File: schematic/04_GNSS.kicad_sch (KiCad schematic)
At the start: 12 parts, among them J5 U.FL_GNSS, J6 SWF_GNSS

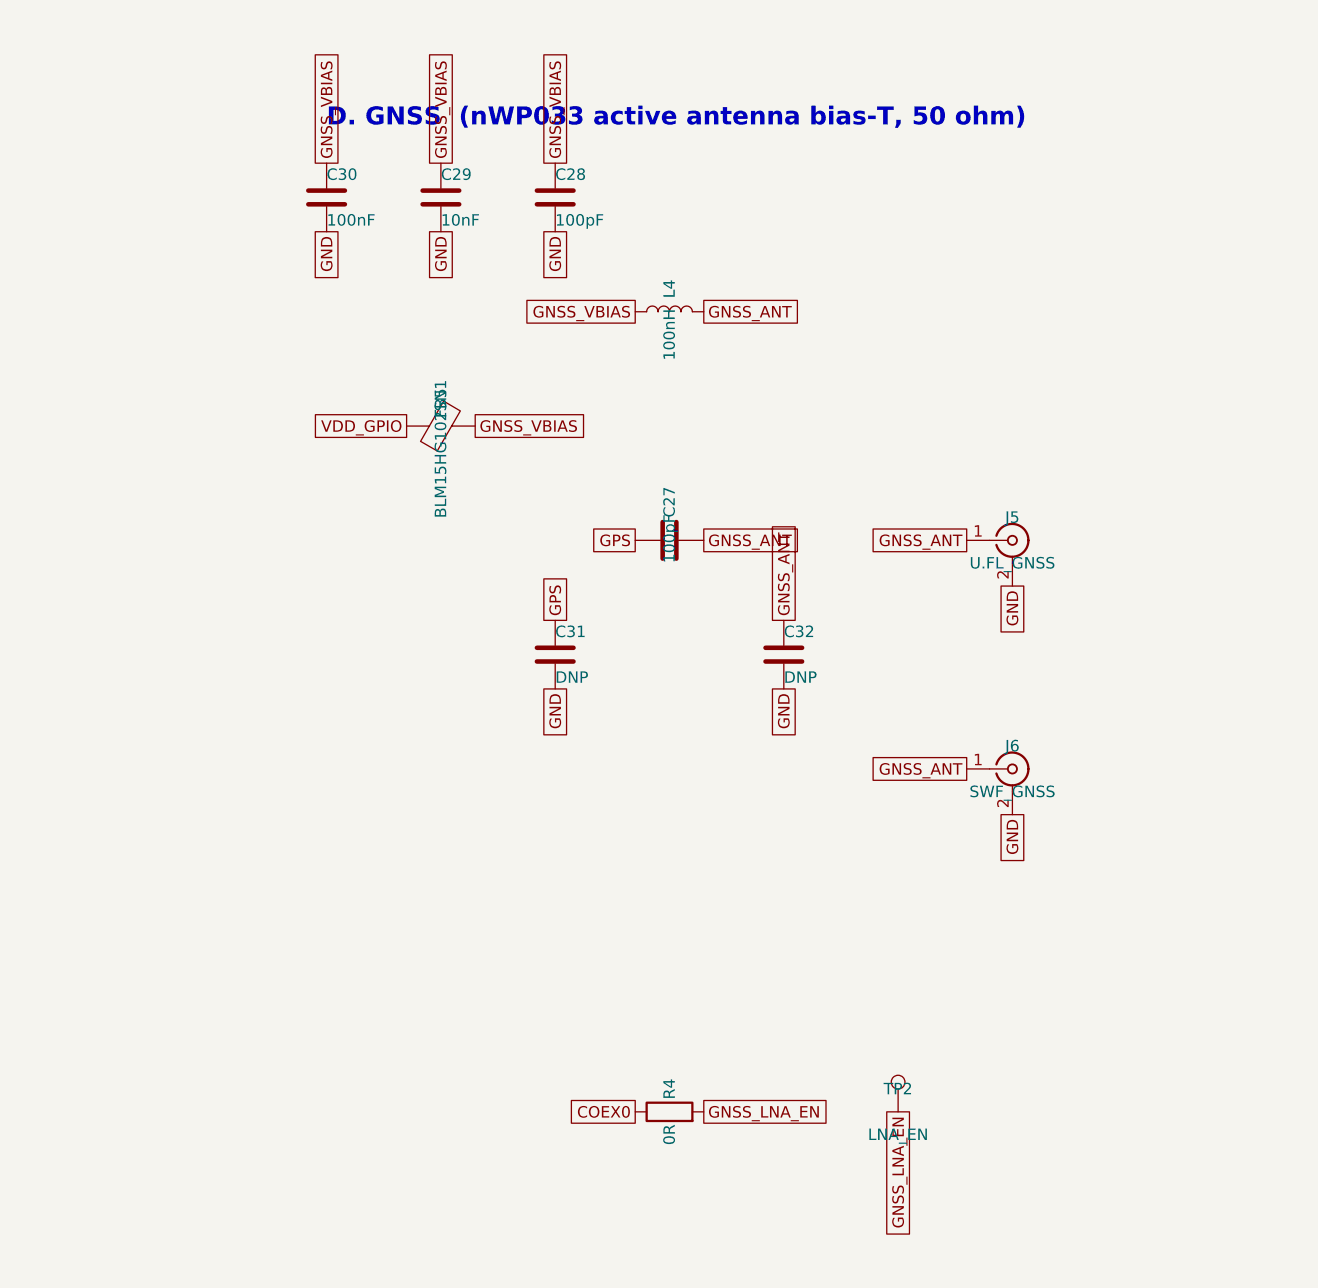
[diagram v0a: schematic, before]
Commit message: Schematic: GNSS COEX0 bias switch, 3.3V VDD_GPIO, DNP RF shunts
- Add U3 TPS22919DCKR on 04_GNSS (COEX0-gated bias); FB5 0402
- Swap U2 to TLV73333 (3.3 V VDD_GPIO); DNP Class-C shunt caps
- Quarantine leftover schematics/; remove stale ERC rpt
- Add PM/DFM/RF/schematic/layout review docs under docs/
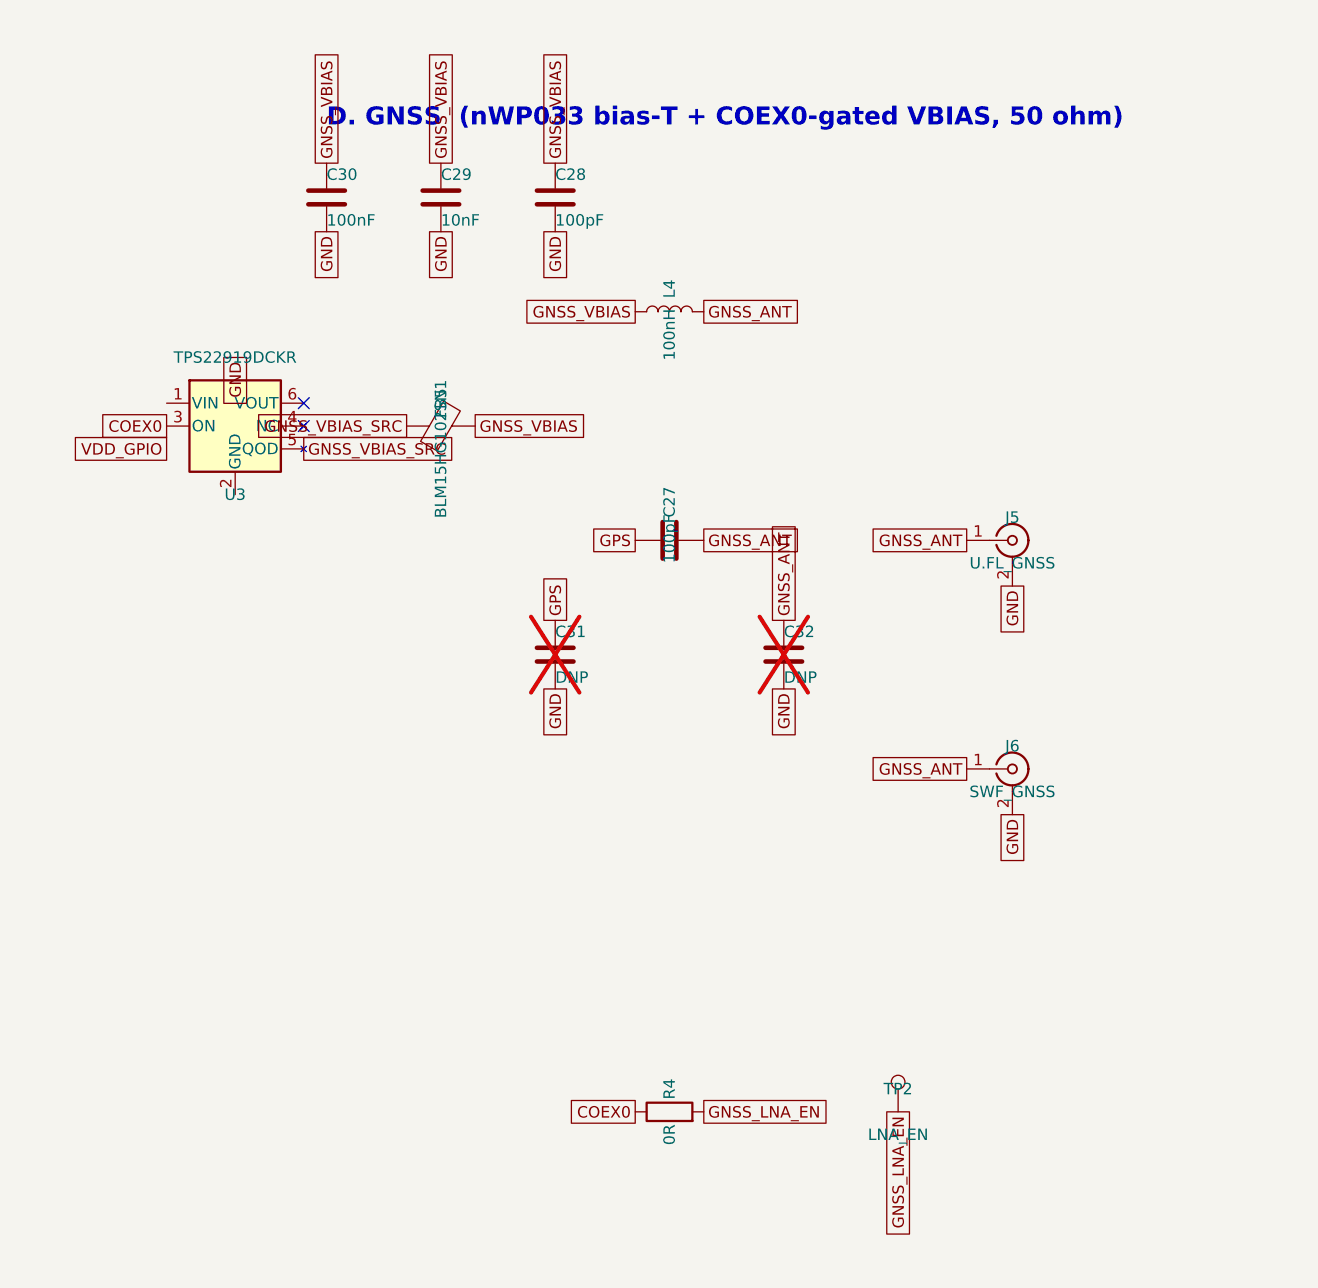
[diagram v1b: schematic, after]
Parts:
- added U3: TPS22919DCKR, Package_TO_SOT_SMD:SOT-363_SC-70-6, symbol power_switch:TPS22919DCK
- C31, C32: now not fitted; now left out of the parts list
- FB5: footprint Inductor_SMD:L_0603_1608Metric -> Inductor_SMD:L_0402_1005Metric
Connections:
- net COEX0: now also U3.3 (ON)
- net VDD_GPIO: no longer FB5.1
- new net GNSS_VBIAS_SRC: FB5.1, U3.5 (QOD)
- no-connect marks 0 -> 2
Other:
- note added: "D. GNSS (nWP033 bias-T + COEX0-gated VBIAS, 50 ohm)"
- note removed: "D. GNSS (nWP033 active antenna bias-T, 50 ohm)"
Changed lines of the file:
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@@
 			)
 		)
-		(property "Footprint" "Inductor_SMD:L_0603_1608Metric"
+		(property "Footprint" "Inductor_SMD:L_0402_1005Metric"
 			(at 38.1 39.878 90)
 			(hide yes)
@@
 		(unit 1)
 		(exclude_from_sim no)
-		(in_bom yes)
+		(in_bom no)
 		(on_board yes)
-		(dnp no)
+		(dnp yes)
 		(property "Reference" "C31"
 			(at 50.8 60.96 0)
@@
 		(unit 1)
 		(exclude_from_sim no)
-		(in_bom yes)
+		(in_bom no)
 		(on_board yes)
-		(dnp no)
+		(dnp yes)
 		(property "Reference" "C32"
 			(at 76.2 60.96 0)
@@
 		)
 	)
-	(global_label "VDD_GPIO"
+	(global_label "GNSS_VBIAS_SRC"
 		(at 34.29 38.1 180)
 		(effects
@@
 		)
 	)
-	(text "D. GNSS  (nWP033 active antenna bias-T, 50 ohm)"
+	(symbol
+		(lib_id "power_switch:TPS22919DCK")
+		(at 15.24 38.1 0)
+		(unit 1)
+		(exclude_from_sim no)
+		(in_bom yes)
+		(on_board yes)
+		(dnp no)
+		(property "Reference" "U3"
+			(at 15.24 45.72 0)
+			(show_name no)
+			(do_not_autoplace no)
+			(effects
+				(font
+					(size 1.27 1.27)
+				)
+			)
+		)
+		(property "Value" "TPS22919DCKR"
+			(at 15.24 30.48 0)
+			(show_name no)
+			(do_not_autoplace no)
+			(effects
+				(font
+					(size 1.27 1.27)
+				)
+			)
+		)
+		(property "Footprint" "Package_TO_SOT_SMD:SOT-363_SC-70-6"
+			(at 15.24 38.1 0)
+			(hide yes)
+			(show_name no)
+			(do_not_autoplace no)
+			(effects
+				(font
+					(size 1.27 1.27)
+				)
+			)
+		)
+		(property "Datasheet" "https://www.ti.com/lit/ds/symlink/tps22919.pdf"
+			(at 15.24 38.1 0)
+			(hide yes)
+			(show_name no)
+			(do_not_autoplace no)
+			(effects
+				(font
+					(size 1.27 1.27)
+				)
+			)
+		)
+		(property "Description" "GNSS VBIAS high-side load switch; EN=COEX0"
+			(at 15.24 38.1 0)
+			(hide yes)
+			(show_name no)
+			(do_not_autoplace no)
+			(effects
+				(font
+					(size 1.27 1.27)
+				)
+			)
+		)
+		(pin "1"
+		)
+		(pin "2"
+		)
+		(pin "3"
+		)
+		(pin "4"
+		)
+		(pin "5"
+		)
+		(pin "6"
+		)
+		(instances
+			(project "nRF9161-DEV-BOARD"
+				(path "/320bf8b0-a48d-42b3-ac88-adf50757caa1"
+					(reference "U3")
+					(unit 1)
+				)
+			 (path "/e1caf6a7-e2a0-4ff1-8424-4d92c0348b6b/846499a2-d5e5-4b82-8bbd-f42a5b8cc356" (reference "U3") (unit 1)) (path "/e1caf6a7-e2a0-4ff1-8424-4d92c0348b6b/4f557c02-0258-45cb-8da4-f63d73173d91" (reference "U3") (unit 1)))
+		)
+	)
+	(global_label "VDD_GPIO"
+		(at 7.62 40.64 180)
+		(effects
+			(font
+				(size 1.27 1.27)
+			)
+			(justify right)
+		)
+	)
+	(global_label "COEX0"
+		(at 7.62 38.1 180)
+		(effects
+			(font
+				(size 1.27 1.27)
+			)
+			(justify right)
+		)
+	)
+	(global_label "GNSS_VBIAS_SRC"
+		(at 22.86 40.64 0)
+		(effects
+			(font
+				(size 1.27 1.27)
+			)
+			(justify left)
+		)
+	)
+	(global_label "GND"
+		(at 15.24 30.48 270)
+		(effects
+			(font
+				(size 1.27 1.27)
+			)
+			(justify right)
+		)
+	)
+	(no_connect
+		(at 22.86 38.1)
+	)
+	(no_connect
+		(at 22.86 35.56)
+	)
+	(text "D. GNSS  (nWP033 bias-T + COEX0-gated VBIAS, 50 ohm)"
 		(exclude_from_sim no)
 		(at 25.4 5.08 0)

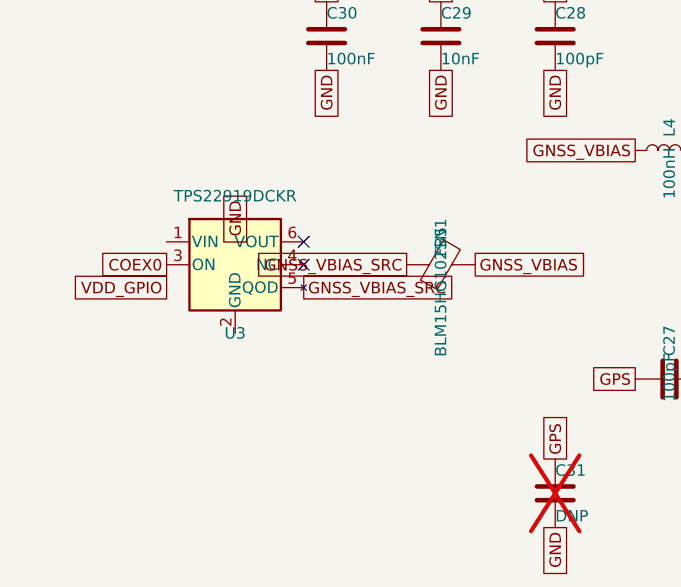
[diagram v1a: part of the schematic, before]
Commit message: Schematic: fix U3 TPS22919 pin labels on GNSS sheet (0 ERC errors)
Correct Y-flipped label/wire/no_connect placement so VIN/VOUT/GND/ON land on the right nets. Archive post-fix netlist and ERC; update schematic review notes.
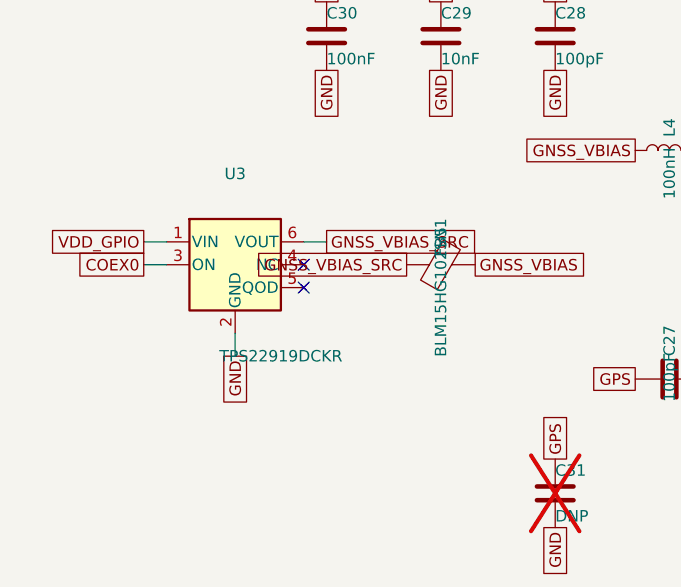
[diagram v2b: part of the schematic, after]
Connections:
- net GND: now also U3.2 (GND)
- net GNSS_VBIAS_SRC: now also U3.6 (VOUT); no longer U3.5 (QOD)
- net VDD_GPIO: now also U3.1 (VIN)
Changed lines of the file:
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@@
 		(dnp no)
 		(property "Reference" "U3"
-			(at 15.24 45.72 0)
+			(at 15.24 28.0 0)
 			(show_name no)
 			(do_not_autoplace no)
@@
 		)
 		(property "Value" "TPS22919DCKR"
-			(at 15.24 30.48 0)
+			(at 20.32 48.26 0)
 			(show_name no)
 			(do_not_autoplace no)
@@
 		)
 	)
+	(wire
+		(pts
+			(xy 7.62 35.56)
+			(xy 5.08 35.56)
+		)
+		(stroke
+			(width 0)
+			(type default)
+		)
+	)
+	(wire
+		(pts
+			(xy 7.62 38.1)
+			(xy 5.08 38.1)
+		)
+		(stroke
+			(width 0)
+			(type default)
+		)
+	)
+	(wire
+		(pts
+			(xy 22.86 35.56)
+			(xy 25.4 35.56)
+		)
+		(stroke
+			(width 0)
+			(type default)
+		)
+	)
+	(wire
+		(pts
+			(xy 15.24 45.72)
+			(xy 15.24 48.26)
+		)
+		(stroke
+			(width 0)
+			(type default)
+		)
+	)
 	(global_label "VDD_GPIO"
-		(at 7.62 40.64 180)
+		(at 5.08 35.56 180)
 		(effects
 			(font
@@
 	)
 	(global_label "COEX0"
-		(at 7.62 38.1 180)
+		(at 5.08 38.1 180)
 		(effects
 			(font
@@
 	)
 	(global_label "GNSS_VBIAS_SRC"
-		(at 22.86 40.64 0)
+		(at 25.4 35.56 0)
 		(effects
 			(font
@@
 	)
 	(global_label "GND"
-		(at 15.24 30.48 270)
+		(at 15.24 48.26 270)
 		(effects
 			(font
@@
 	)
 	(no_connect
-		(at 22.86 35.56)
+		(at 22.86 40.64)
 	)
 	(text "D. GNSS  (nWP033 bias-T + COEX0-gated VBIAS, 50 ohm)"

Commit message: Exclude JP1, JP2, TP1-TP20 from BOM (attrs only, sch+pcb)
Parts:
- TP2: now left out of the parts list
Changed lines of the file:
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@@
 		(unit 1)
 		(exclude_from_sim no)
-		(in_bom yes)
+		(in_bom no)
 		(on_board yes)
 		(dnp no)

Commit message: v2: simplify to UART modem module (J20 host header, LXC translators); remove J1, J3, J6, J9-J18, optional parts
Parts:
- removed J6: SWF_GNSS, Board:Murata_MM8130-2600_SWF, symbol Connector:Conn_Coaxial
- removed R4: 0R, Resistor_SMD:R_0402_1005Metric, symbol Device:R
- removed TP2: LNA_EN, TestPoint:TestPoint_Pad_D1.5mm, symbol Connector:TestPoint

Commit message: v2 BOM: apply footprint-consistent MPNs + LCSC IDs, JLC BOM, audit reports (U4 footprint pending Layout)
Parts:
- C27: LCSC (none) -> C76922; MPN (none) -> GRM0335C1H101JA01D; Manufacturer (none) -> Murata
- C28: LCSC (none) -> C77177; MPN (none) -> GRM1555C1H101JA01D; Manufacturer (none) -> Murata
- C29: LCSC (none) -> C15195; MPN (none) -> CL05B103KB5NNNC; Manufacturer (none) -> Samsung Electro-Mechanics
- C30: LCSC (none) -> C1525; MPN (none) -> CL05B104KO5NNNC; Manufacturer (none) -> Samsung Electro-Mechanics
- FB5: LCSC (none) -> C76889; MPN (none) -> BLM15HG102SN1D; Manufacturer (none) -> Murata
- J5: LCSC (none) -> C88373; MPN (none) -> U.FL-R-SMT-1(10); Manufacturer (none) -> Hirose
- L4: LCSC (none) -> C86130; MPN (none) -> LQW15ANR10J00D; Manufacturer (none) -> Murata
- U3: LCSC (none) -> C2149796; MPN (none) -> TPS22919DCKR; Manufacturer (none) -> Texas Instruments
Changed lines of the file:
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@@
+			)
+		)
+		(property "MPN" "GRM0335C1H101JA01D"
+			(at 63.5 50.8 90)
+			(hide yes)
+			(effects
+				(font
+					(size 1.27 1.27)
+				)
+			)
+		)
+		(property "LCSC" "C76922"
+			(at 63.5 50.8 90)
+			(hide yes)
+			(effects
+				(font
+					(size 1.27 1.27)
+				)
+			)
+		)
+		(property "Manufacturer" "Murata"
+			(at 63.5 50.8 90)
+			(hide yes)
+			(effects
+				(font
+					(size 1.27 1.27)
+				)
 			)
 		)
@@
 			)
 		)
+		(property "MPN" "LQW15ANR10J00D"
+			(at 63.5 25.4 90)
+			(hide yes)
+			(effects
+				(font
+					(size 1.27 1.27)
+				)
+			)
+		)
+		(property "LCSC" "C86130"
+			(at 63.5 25.4 90)
+			(hide yes)
+			(effects
+				(font
+					(size 1.27 1.27)
+				)
+			)
+		)
+		(property "Manufacturer" "Murata"
+			(at 63.5 25.4 90)
+			(hide yes)
+			(effects
+				(font
+					(size 1.27 1.27)
+				)
+			)
+		)
 		(pin "1"
 		)
@@
 			)
 		)
+		(property "MPN" "GRM1555C1H101JA01D"
+			(at 50.8 12.7 0)
+			(hide yes)
+			(effects
+				(font
+					(size 1.27 1.27)
+				)
+			)
+		)
+		(property "LCSC" "C77177"
+			(at 50.8 12.7 0)
+			(hide yes)
+			(effects
+				(font
+					(size 1.27 1.27)
+				)
+			)
+		)
+		(property "Manufacturer" "Murata"
+			(at 50.8 12.7 0)
+			(hide yes)
+			(effects
+				(font
+					(size 1.27 1.27)
+				)
+			)
+		)
 		(pin "1"
 		)
@@
 			)
 		)
+		(property "MPN" "CL05B103KB5NNNC"
+			(at 38.1 12.7 0)
+			(hide yes)
+			(effects
+				(font
+					(size 1.27 1.27)
+				)
+			)
+		)
+		(property "LCSC" "C15195"
+			(at 38.1 12.7 0)
+			(hide yes)
+			(effects
+				(font
+					(size 1.27 1.27)
+				)
+			)
+		)
+		(property "Manufacturer" "Samsung Electro-Mechanics"
+			(at 38.1 12.7 0)
+			(hide yes)
+			(effects
+				(font
+					(size 1.27 1.27)
+				)
+			)
+		)
 		(pin "1"
 		)
@@
 			)
 		)
+		(property "MPN" "CL05B104KO5NNNC"
+			(at 25.4 12.7 0)
+			(hide yes)
+			(effects
+				(font
+					(size 1.27 1.27)
+				)
+			)
+		)
+		(property "LCSC" "C1525"
+			(at 25.4 12.7 0)
+			(hide yes)
+			(effects
+				(font
+					(size 1.27 1.27)
+				)
+			)
+		)
+		(property "Manufacturer" "Samsung Electro-Mechanics"
+			(at 25.4 12.7 0)
+			(hide yes)
+			(effects
+				(font
+					(size 1.27 1.27)
+				)
+			)
+		)
 		(pin "1"
 		)
@@
 			)
 		)
+		(property "MPN" "BLM15HG102SN1D"
+			(at 38.1 38.1 90)
+			(hide yes)
+			(effects
+				(font
+					(size 1.27 1.27)
+				)
+			)
+		)
+		(property "LCSC" "C76889"
+			(at 38.1 38.1 90)
+			(hide yes)
+			(effects
+				(font
+					(size 1.27 1.27)
+				)
+			)
+		)
+		(property "Manufacturer" "Murata"
+			(at 38.1 38.1 90)
+			(hide yes)
+			(effects
+				(font
+					(size 1.27 1.27)
+				)
+			)
+		)
 		(pin "1"
 		)
@@
 			)
 		)
+		(property "MPN" "U.FL-R-SMT-1(10)"
+			(at 101.6 50.8 0)
+			(hide yes)
+			(effects
+				(font
+					(size 1.27 1.27)
+				)
+			)
+		)
+		(property "LCSC" "C88373"
+			(at 101.6 50.8 0)
+			(hide yes)
+			(effects
+				(font
+					(size 1.27 1.27)
+				)
+			)
+		)
+		(property "Manufacturer" "Hirose"
+			(at 101.6 50.8 0)
+			(hide yes)
+			(effects
+				(font
+					(size 1.27 1.27)
+				)
+			)
+		)
 		(pin "1"
 		)
@@
 			(effects
 				(font
+					(size 1.27 1.27)
+				)
+			)
+		)
+		(property "MPN" "TPS22919DCKR"
+			(at 15.24 38.1 0)
+			(hide yes)
+			(effects
+				(font
+					(size 1.27 1.27)
+				)
+			)
+		)
+		(property "LCSC" "C2149796"
+			(at 15.24 38.1 0)
+			(hide yes)
+			(effects
+				(font
+					(size 1.27 1.27)
+				)
+			)
+		)
+		(property "Manufacturer" "Texas Instruments"
+			(at 15.24 38.1 0)
+			(hide yes)
+			(effects
+				(font
